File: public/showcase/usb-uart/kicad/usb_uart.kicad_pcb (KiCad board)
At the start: 4 copper layers, 50.4 x 38.3 mm, 40 parts, among them J1 12401610E4#2A, J2 UART1, J3 FLOW1, J4 RS485, U1 CH342F, U2 LDO, U3 THVD1450D

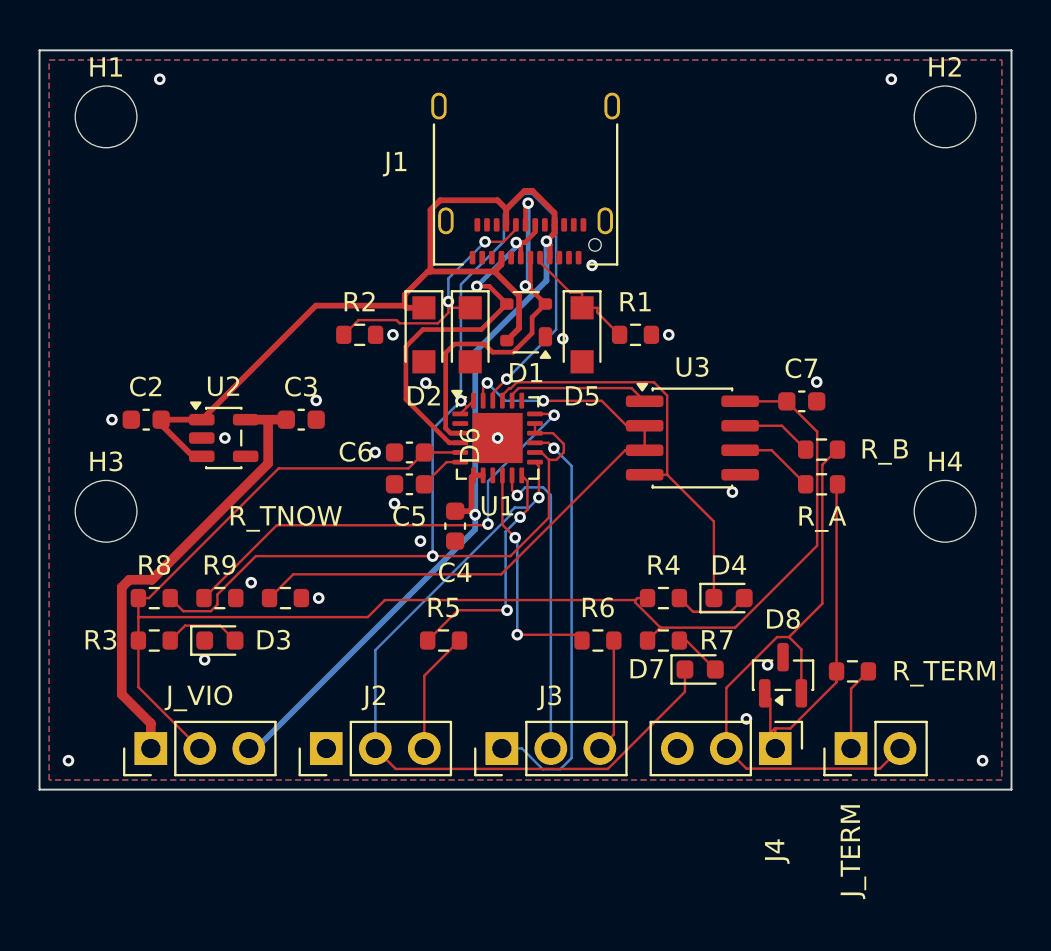
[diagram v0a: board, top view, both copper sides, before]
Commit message: NOISSUE - Show the two-layer USB UART board
Replace the revision B showcase (50.5 x 38.4 mm, four layers, J_TERM
and an RS-485 surge network) with the two-layer revision A published
in absmach/synth#103 at 4ab0eb9.

- kicad/, source, placement sidecar and reports from that revision.
- Layer tabs drop to top and bottom; the showcase check accepts 2 or 4
  copper layers.
- Regenerate the layer SVGs, schematic SVG, 3D render, GLB, STEP and OG
  image; drop the schematic sidecar and the revision B brief.
- Rewrite QUALIFICATION.md, the prompt and the page metadata for
  revision A: 41.5 x 32.23 mm, 26 nets, 271 segments, 38 vias,
  507.7 mm, no impedance target on the USB pair, fixed RS-485
  termination and no external TVS on A/B.
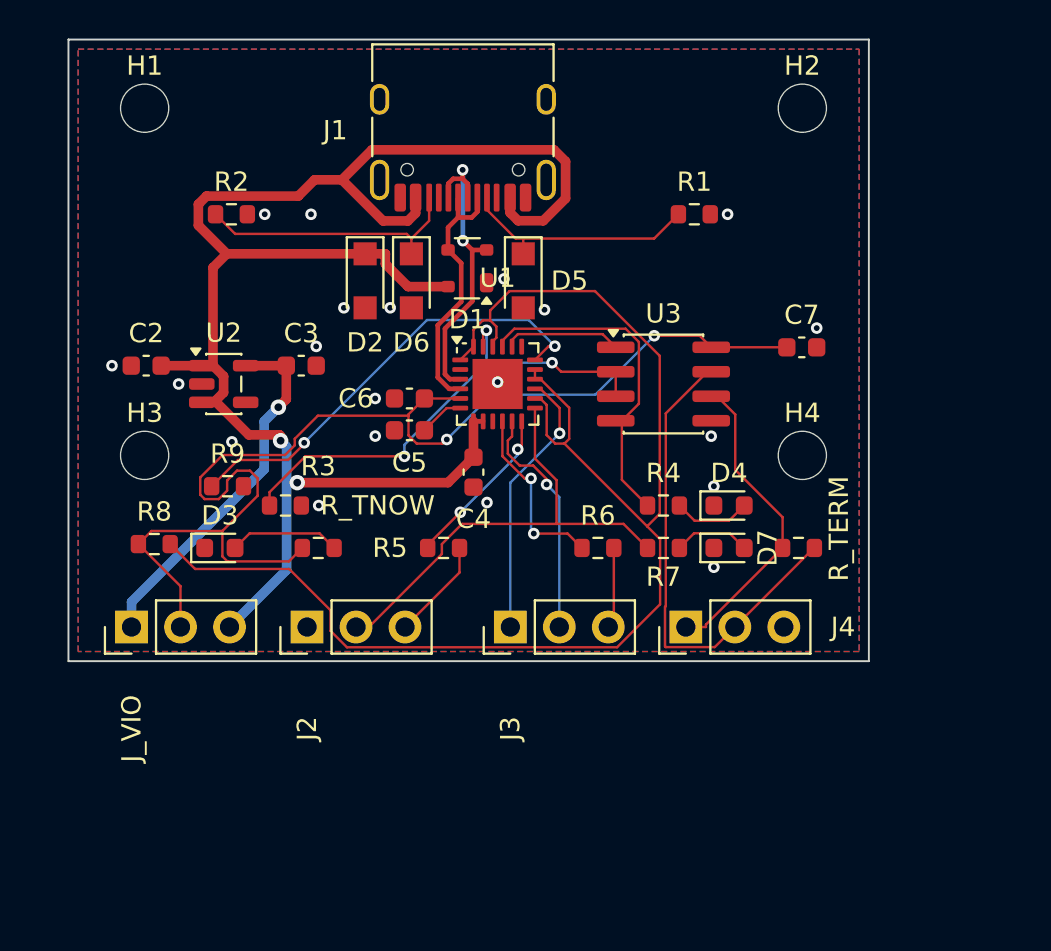
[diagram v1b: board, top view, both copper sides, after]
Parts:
- removed D8: TVS, Package_TO_SOT_SMD:SOT-23
- removed J_TERM: TERM, Connector_PinHeader_2.54mm:PinHeader_1x02_P2.54mm_Vertical
- removed R_A, R_B: 10ohm, Resistor_SMD:R_0603_1608Metric
- H1, H2, H3, H4: footprint MountingHole:MountingHole_3.2mm_M3 -> MountingHole:MountingHole_2.5mm
- J1: value 12401610E4#2A -> TYPE-C-31-M-12; footprint Connector_USB:USB_C_Receptacle_Amphenol_12401610E4-2A -> Connector_USB:USB_C_Receptacle_HRO_TYPE-C-31-M-12
- moved R3 9.76 mm to (14.5, 25.8)
- moved R2 9.13 mm to (10.0, 8.50)
- moved H4 7.95 mm to (39.6, 21.0)
- moved J4 7.82 mm to (33.6, 29.9), turned to 90 degrees
- moved H2 7.41 mm to (39.6, 3.00)
- moved R_TERM 6.99 mm to (39.4, 25.8)
- moved R1 6.95 mm to (34.0, 8.50)
- moved D7 6.48 mm to (35.8, 25.8)
- moved J2 6.38 mm to (13.9, 29.9)
- moved J_VIO 6.38 mm to (4.82, 29.9)
- moved J3 6.32 mm to (24.5, 29.9)
- moved R9 5.81 mm to (9.80, 22.6)
- moved D3 4.80 mm to (9.40, 25.8)
- moved R5 4.80 mm to (21.0, 25.8)
- moved R6 4.80 mm to (29.0, 25.8)
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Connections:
- D4 pad 1: TXD0 -> GND
- D7 pad 1: TXD1 -> GND
- J4 pad 1: RS485_A_BUS -> RS485_A
- J4 pad 2: RS485_B_BUS -> RS485_B
- R4 pad 1: VIO -> TXD0
- R7 pad 1: VIO -> TXD1
- R_TERM pad 1: RS485_A_BUS -> RS485_A
- R_TERM pad 2: RS485_TERM -> RS485_B
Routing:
- net RS485_B_BUS: track 31.3 -> 0.00 mm
- net RS485_B: track 3.91 -> 25.2 mm
- net RS485_A_BUS: track 18.0 -> 0.00 mm
- net VIO: track 79.1 -> 63.0 mm, vias 0 -> 2
- net TXD1: track 38.2 -> 24.6 mm, vias 1 -> 0
- net RS485_A: track 4.13 -> 16.4 mm
- net TNOW0: track 34.0 -> 25.8 mm, vias 2 -> 3
- net DTR1: track 21.8 -> 14.1 mm
- net MODEM_IDLE: track 64.9 -> 72.5 mm, vias 3 -> 0
- net VBUS: track 80.8 -> 87.8 mm
- net USB_DN: track 20.2 -> 13.6 mm, vias 2 -> 0
- net CC1: track 6.53 -> 12.5 mm
- net +3V3: track 23.6 -> 19.0 mm, vias 0 -> 1
- net TXD0: track 22.1 -> 17.6 mm
- net RS485_TERM: track 4.37 -> 0.00 mm
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- removed copper zone on In1.Cu, net GND
- removed copper zone on In2.Cu, net GND
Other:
- board size 50.4 x 38.3 mm -> 41.5 x 32.2 mm
- copper layers 4 -> 2
- net class VBUS_FINE removed

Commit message: NOISSUE - Refresh the showcase to #103 as merged
Copy the board, sidecar, reports and KiCad files from absmach/synth at
de3613e (the merge of #103) and regenerate the GLB, STEP, layer SVGs,
schematic SVG, 3D render and OG image from that board.

- 40.99 x 32.23 mm, 273 segments (213 F.Cu, 60 B.Cu), 43 vias, 515.4 mm.
- KiCad DRC 0 errors and 0 warnings, ERC 0 errors and 1 warning.
- USB pair length, skew and return-path figures, 23 layer-change
  warnings, J1 edge clearance and the TX LED behaviour in the limits.
- Reports name Synth e6455e1, the source_revision in release.json.

Signed-off-by: nyagamunene <stevenyaga2014@gmail.com>
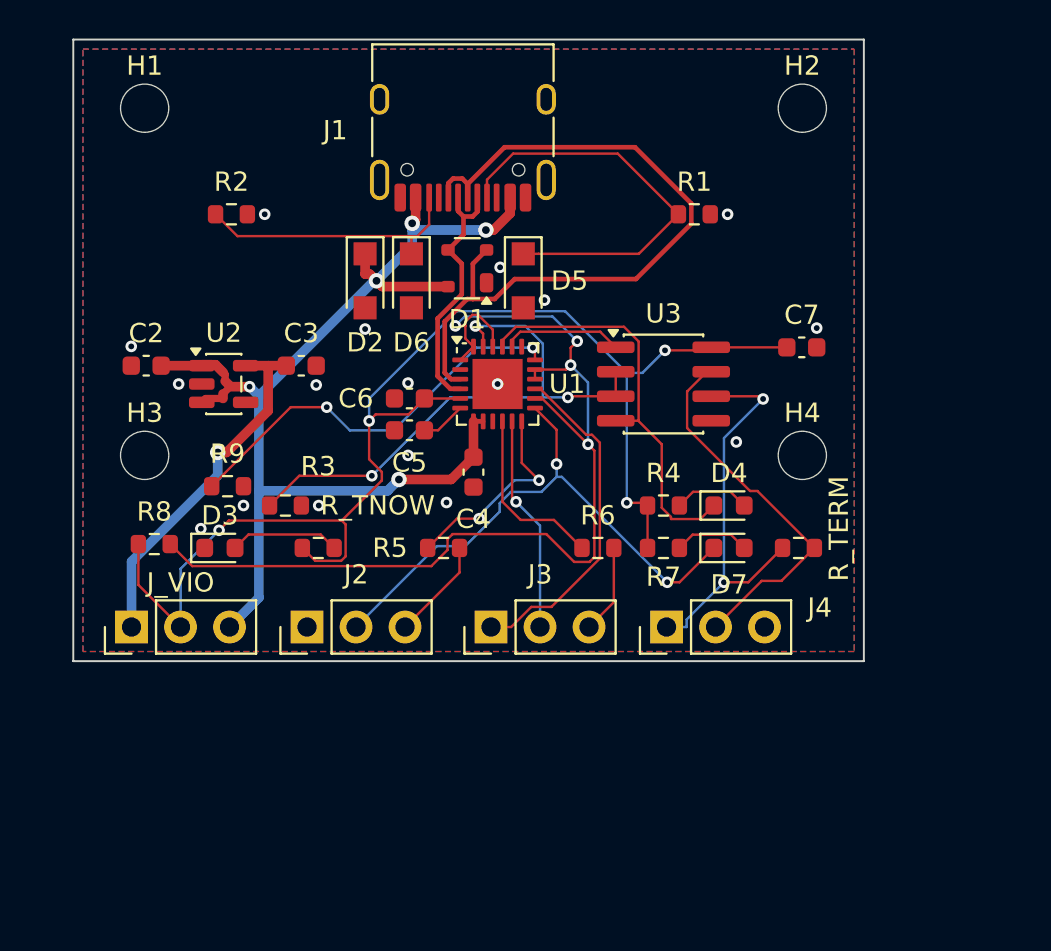
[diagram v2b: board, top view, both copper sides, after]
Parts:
- moved J3 1.00 mm to (23.5, 29.9)
- moved J4 1.00 mm to (32.6, 29.9)
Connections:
- D4 pad 1: GND -> TXD0
- D7 pad 1: GND -> TXD1
- R4 pad 1: TXD0 -> VIO
- R7 pad 1: TXD1 -> VIO
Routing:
- net VBUS: track 87.8 -> 60.4 mm, vias 2 -> 5
- net USB_DP: track 16.2 -> 38.6 mm, vias 2 -> 0
- net MODEM_IDLE: track 72.5 -> 55.0 mm, vias 0 -> 4
- net CC1: track 12.5 -> 21.6 mm
- net VIO: track 63.0 -> 70.3 mm, vias 2 -> 4
- net RS485_B: track 25.2 -> 19.6 mm
- net RS485_A: track 16.4 -> 21.0 mm, vias 0 -> 2
- net TXD1: track 24.6 -> 29.1 mm, vias 0 -> 2
- net TXD0: track 17.6 -> 21.6 mm
- net TNOW0: track 25.8 -> 29.5 mm
- net DTR1: track 14.1 -> 17.6 mm, vias 1 -> 0
- net RXD1_MCU: track 8.58 -> 10.7 mm
- net CTS0_LOW: track 23.3 -> 21.3 mm
- net RTS1: track 12.3 -> 11.3 mm
- net CTS1_MCU: track 9.49 -> 9.28 mm, vias 2 -> 0
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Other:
- board size 41.5 x 32.2 mm -> 41 x 32.2 mm
